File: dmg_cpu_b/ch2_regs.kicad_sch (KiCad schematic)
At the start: 96 parts

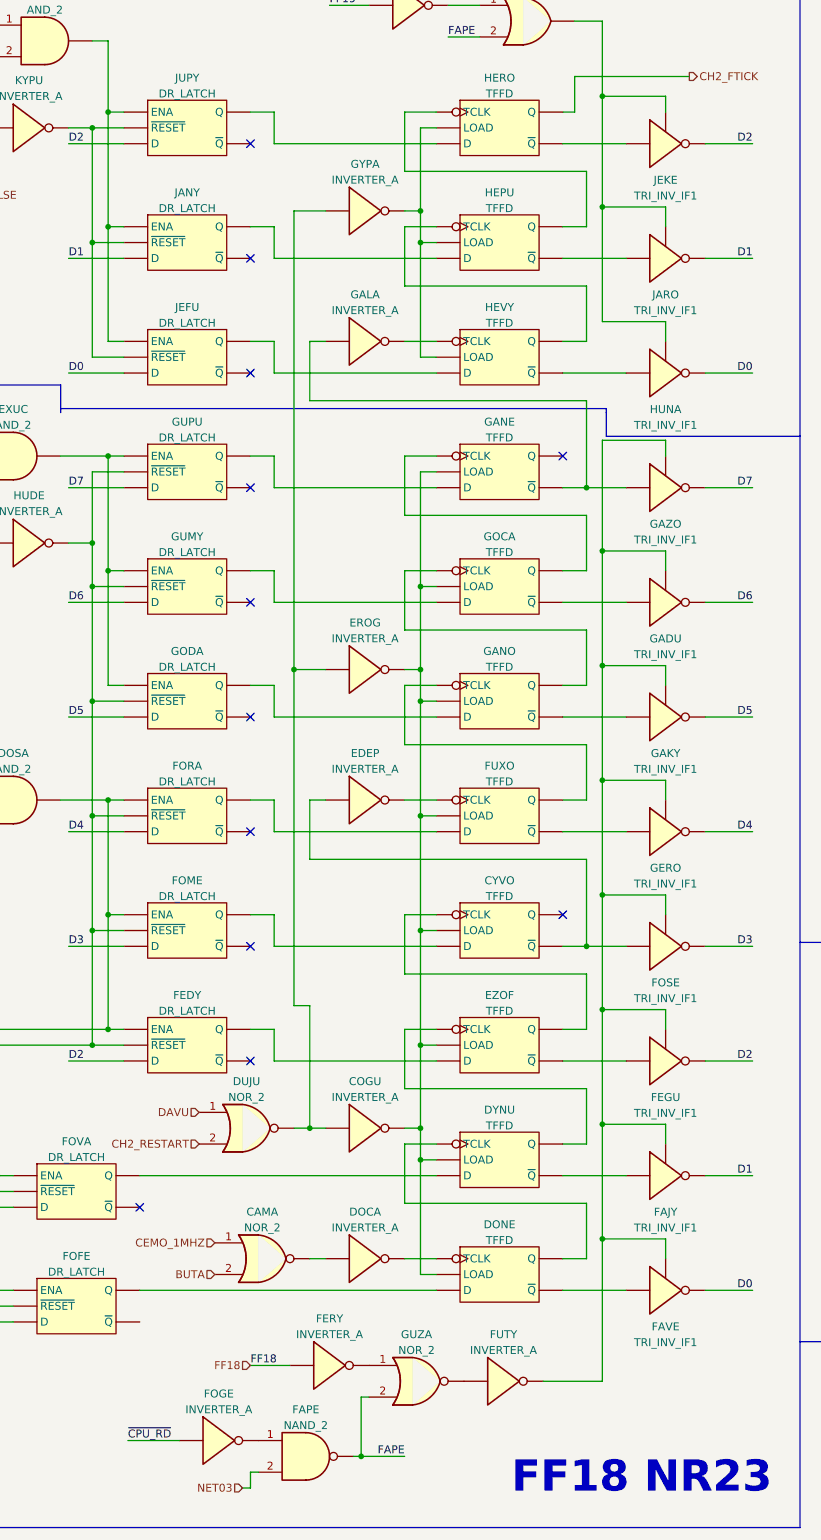
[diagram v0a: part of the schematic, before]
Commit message: Channel 2 + Channel 3 added. Channel 3 fits on 2 sheets.
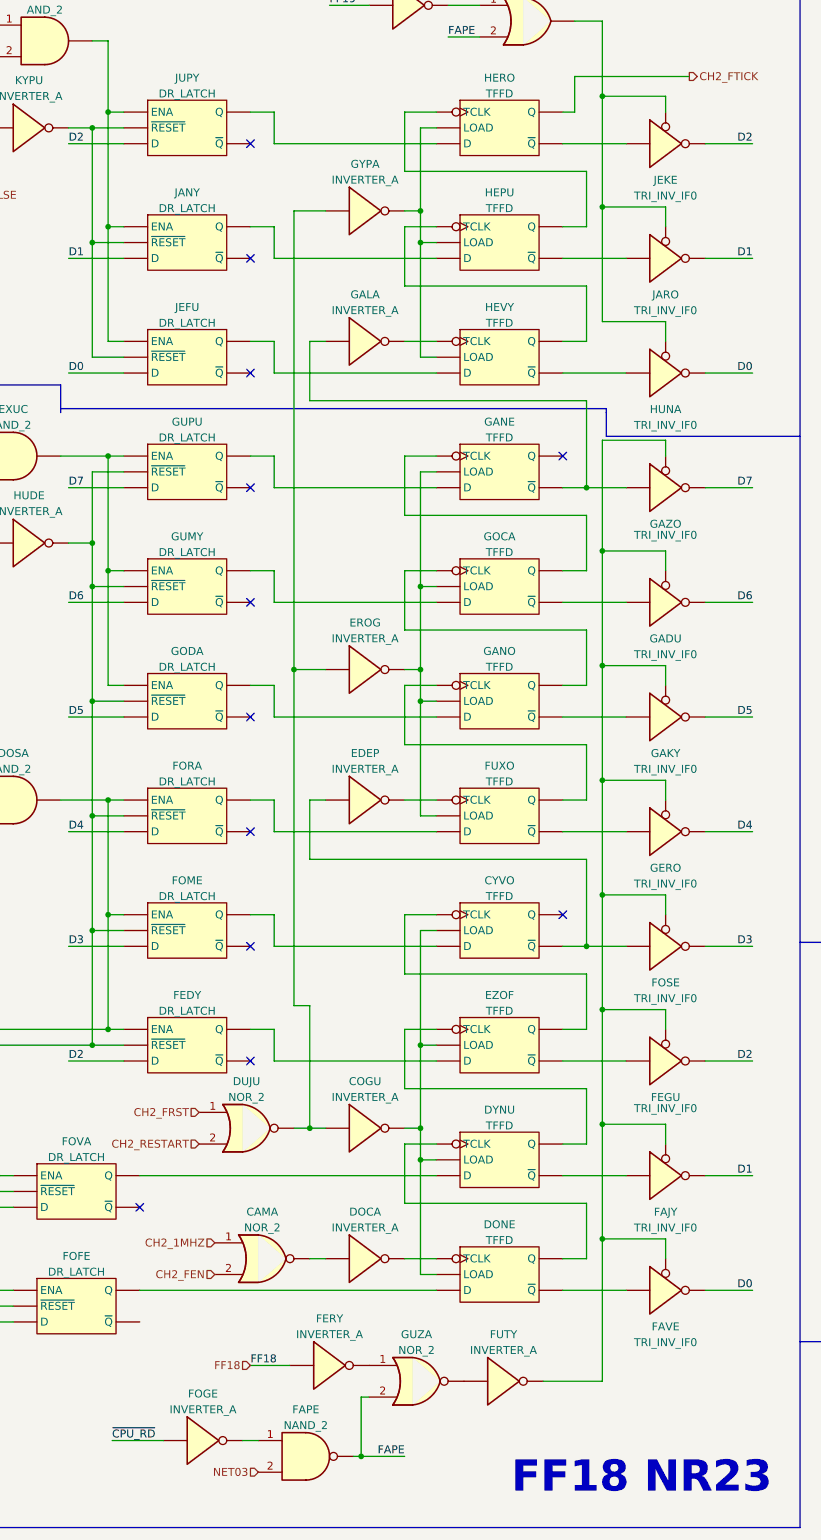
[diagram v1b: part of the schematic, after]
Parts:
- removed FAJY, FAVE, FEGU, FOSE, GADU, GAKY, GAZO, GERO, HUNA, JARO, JEKE: TRI_INV_IF1, symbol DMG_CPU_Cells:TRI_INV_IF1
- added FAJY, FAVE, FEGU, FOSE, GADU, GAKY, GAZO, GERO, HUNA, JARO, JEKE: TRI_INV_IF0, symbol DMG_CPU_Cells:TRI_INV_IF0
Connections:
- net D0: now also FAVE.3, HUNA.3
- net D1: now also FAJY.3, JARO.3
- net D2: now also FEGU.3, JEKE.3
- net D3: now also FOSE.3
- net D4: now also GERO.3
- net D5: now also GAKY.3
- net D6: now also GADU.3
- net D7: now also GAZO.3
- net at EROG.2, FUXO.3 (LOAD), FUXO.4 (LOAD)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: no longer COGU.2, CYVO.3 (LOAD), CYVO.4 (LOAD), DONE.3 (LOAD), DONE.4 (LOAD), DYNU.3 (LOAD), DYNU.4 (LOAD), EZOF.3 (LOAD), EZOF.4 (LOAD)
- net at GOCA.6 (~{Q}): now also GADU.2
- net at FUTY.2: now also FAJY.1 (~{ENA}), FAVE.1 (~{ENA}), FEGU.1 (~{ENA}), FOSE.1 (~{ENA}), GADU.1 (~{ENA}), GAKY.1 (~{ENA}), GAZO.1 (~{ENA}), GERO.1 (~{ENA})
- net at GANO.6 (~{Q}): now also GAKY.2
- net at GALA.1, GANE.6 (~{Q}): now also GAZO.2
- net at HYPO.3: now also HUNA.1 (~{ENA}), JARO.1 (~{ENA}), JEKE.1 (~{ENA})
- net at HERO.6 (~{Q}): now also JEKE.2
- net at CYVO.6 (~{Q}), EDEP.1: now also FOSE.2
- net at EZOF.6 (~{Q}): now also FEGU.2
- net at DONE.6 (~{Q}): now also FAVE.2
- net at HEPU.6 (~{Q}): now also JARO.2
- net at DYNU.6 (~{Q}): now also FAJY.2
- net at HEVY.6 (~{Q}): now also HUNA.2
- net at FUXO.6 (~{Q}): now also GERO.2
- net BUTA renamed CH2_FEN
- net CEMO_1MHZ renamed CH2_1MHZ
- net DAVU renamed CH2_FRST
- new net: COGU.2, CYVO.3 (LOAD), CYVO.4 (LOAD), DONE.3 (LOAD), DONE.4 (LOAD), DYNU.3 (LOAD), DYNU.4 (LOAD), EZOF.3 (LOAD), EZOF.4 (LOAD)
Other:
- moved on the sheet: FOGE

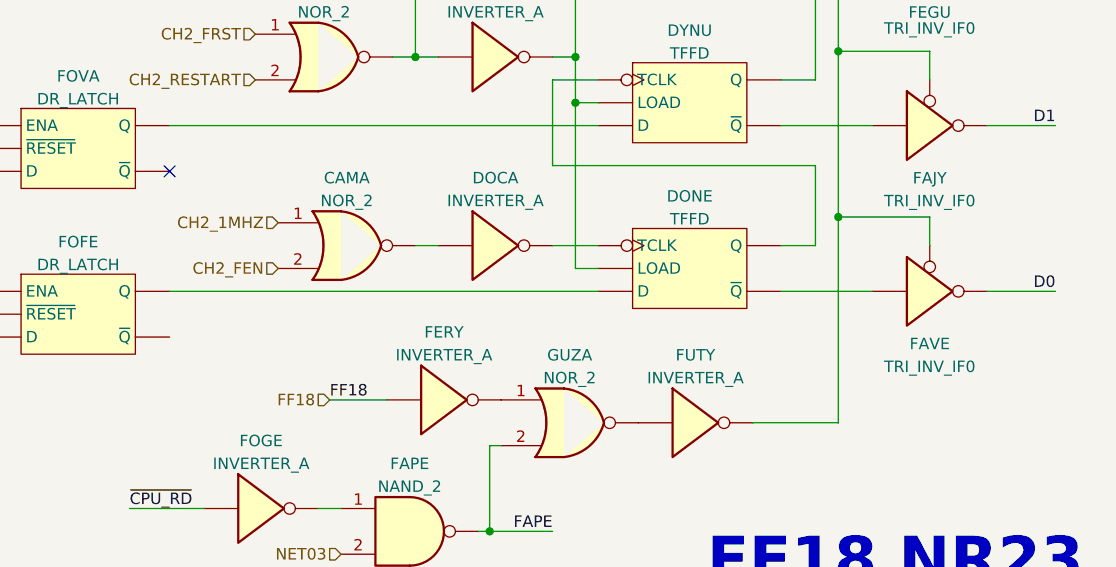
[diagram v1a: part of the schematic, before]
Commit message: Fixes made from issues, channel 4 sheet aded and tidy up of hierarchical APU sheet. Small fixes done here and there when doing ERC.
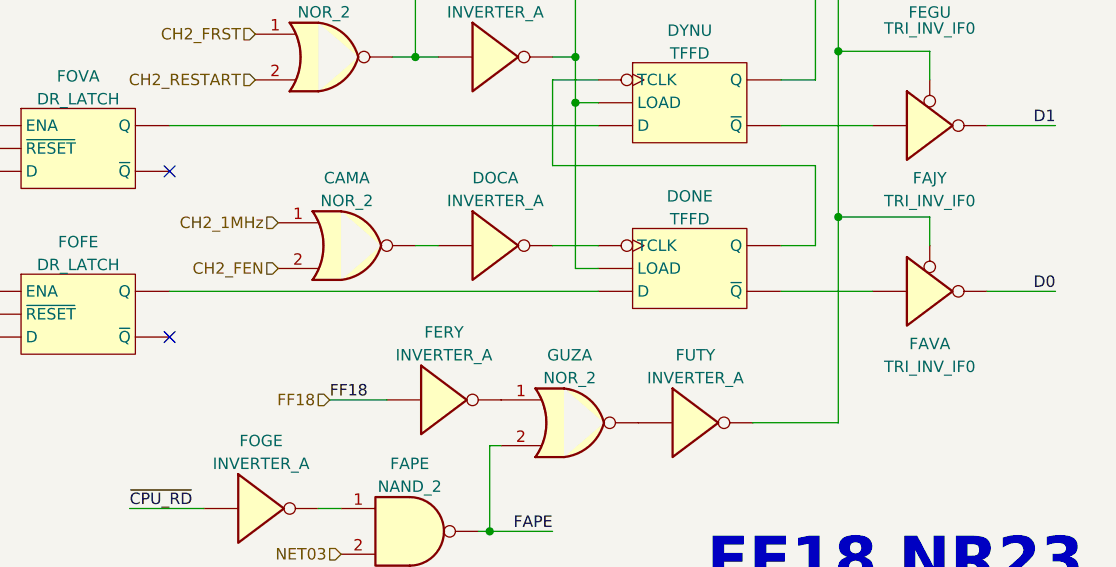
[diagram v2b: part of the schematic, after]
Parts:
- renumbered FAVE to FAVA
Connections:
- net CH2_1MHZ renamed CH2_1MHz
- no-connect marks 14 -> 15
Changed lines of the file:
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@@
   (no_connect (at 205.74 203.2))
   (no_connect (at 205.74 55.88))
+  (no_connect (at 187.96 245.11))
   (no_connect (at 205.74 166.37))
   (no_connect (at 255.905 106.045))
@@
     (effects (font (size 1.27 1.27)) (justify left))
   )
-  (hierarchical_label "CH2_1MHZ" (shape input) (at 200.025 232.41 180)
+  (hierarchical_label "CH2_1MHz" (shape input) (at 200.025 232.41 180)
     (effects (font (size 1.27 1.27)) (justify right))
   )
@@
   (symbol (lib_id "DMG_CPU_Cells:TRI_INV_IF0") (at 272.415 240.03 0) (unit 1)
     (in_bom yes) (on_board yes) (fields_autoplaced)
-    (property "Reference" "FAVE" (id 0) (at 272.415 245.8704 0))
+    (property "Reference" "FAVA" (id 0) (at 272.415 245.8704 0))
     (property "Value" "TRI_INV_IF0" (id 1) (at 272.415 248.4073 0))
     (property "Footprint" "" (id 2) (at 269.875 240.03 0)

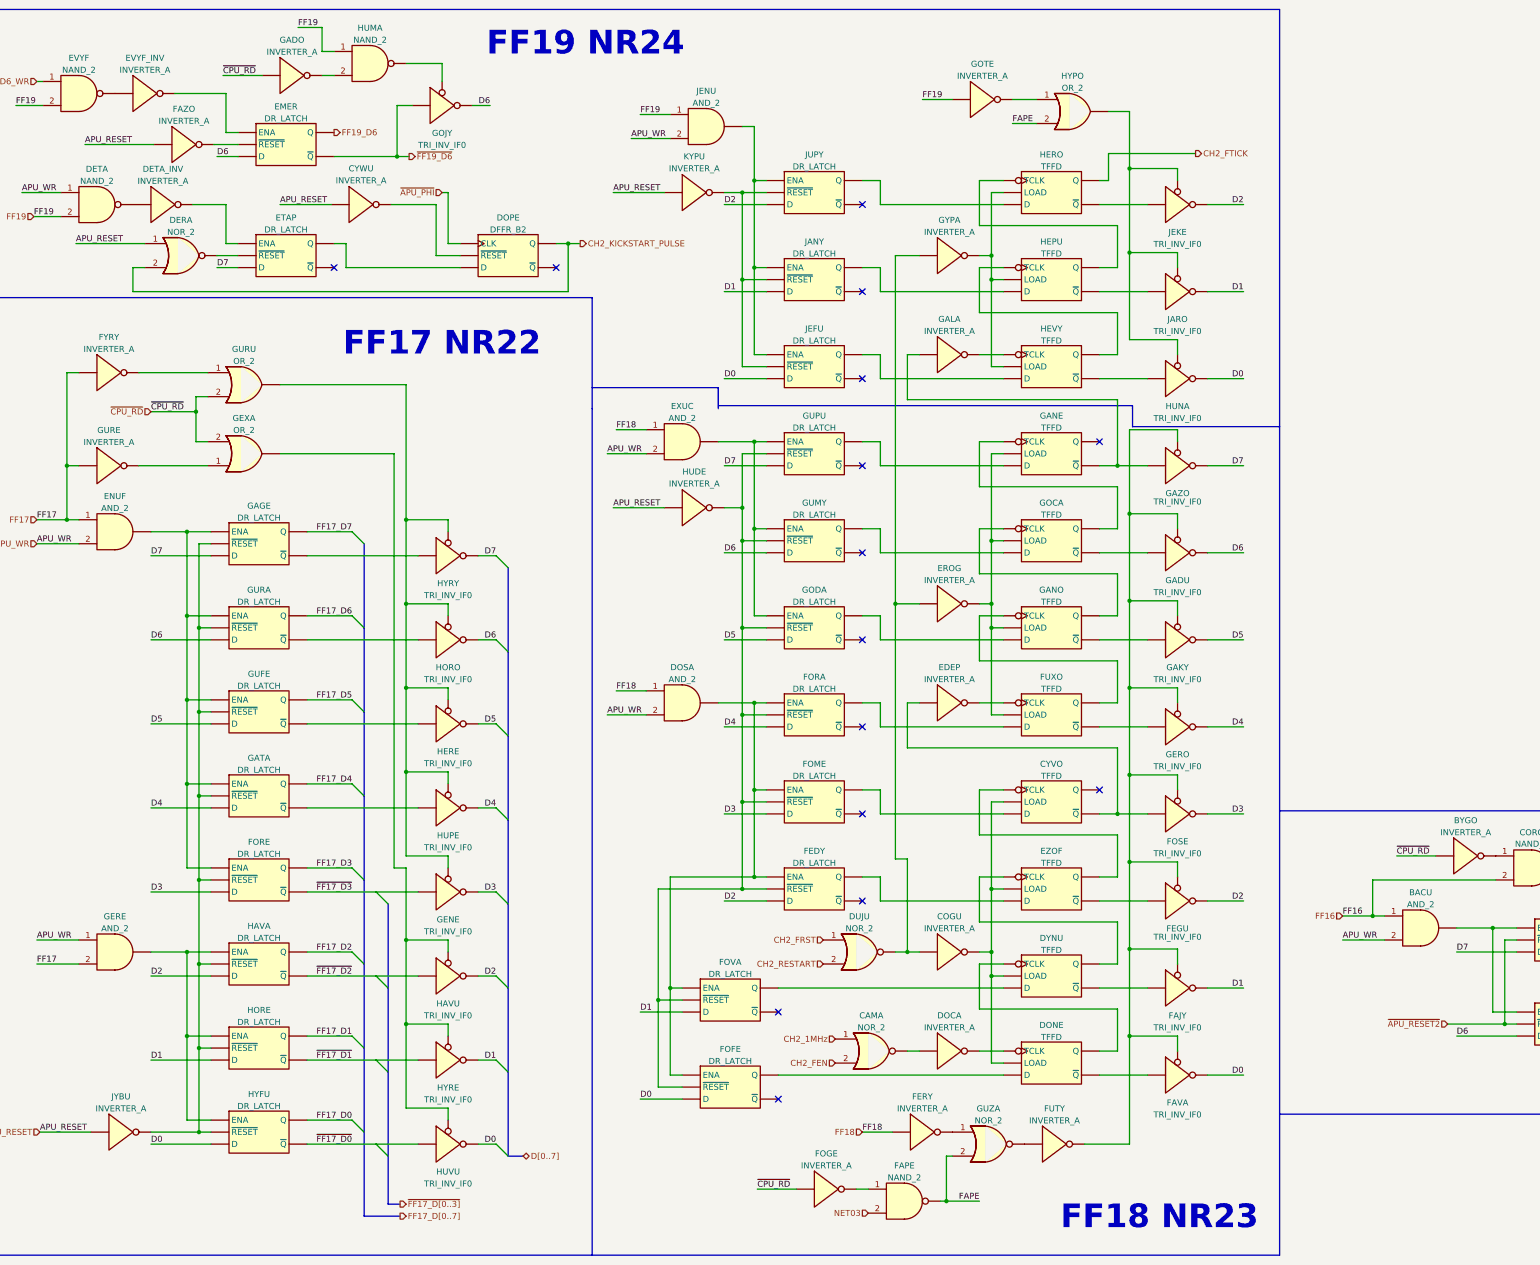
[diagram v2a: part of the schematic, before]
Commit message: Fixes made based on raised issues. PPU decode page added as draft level.
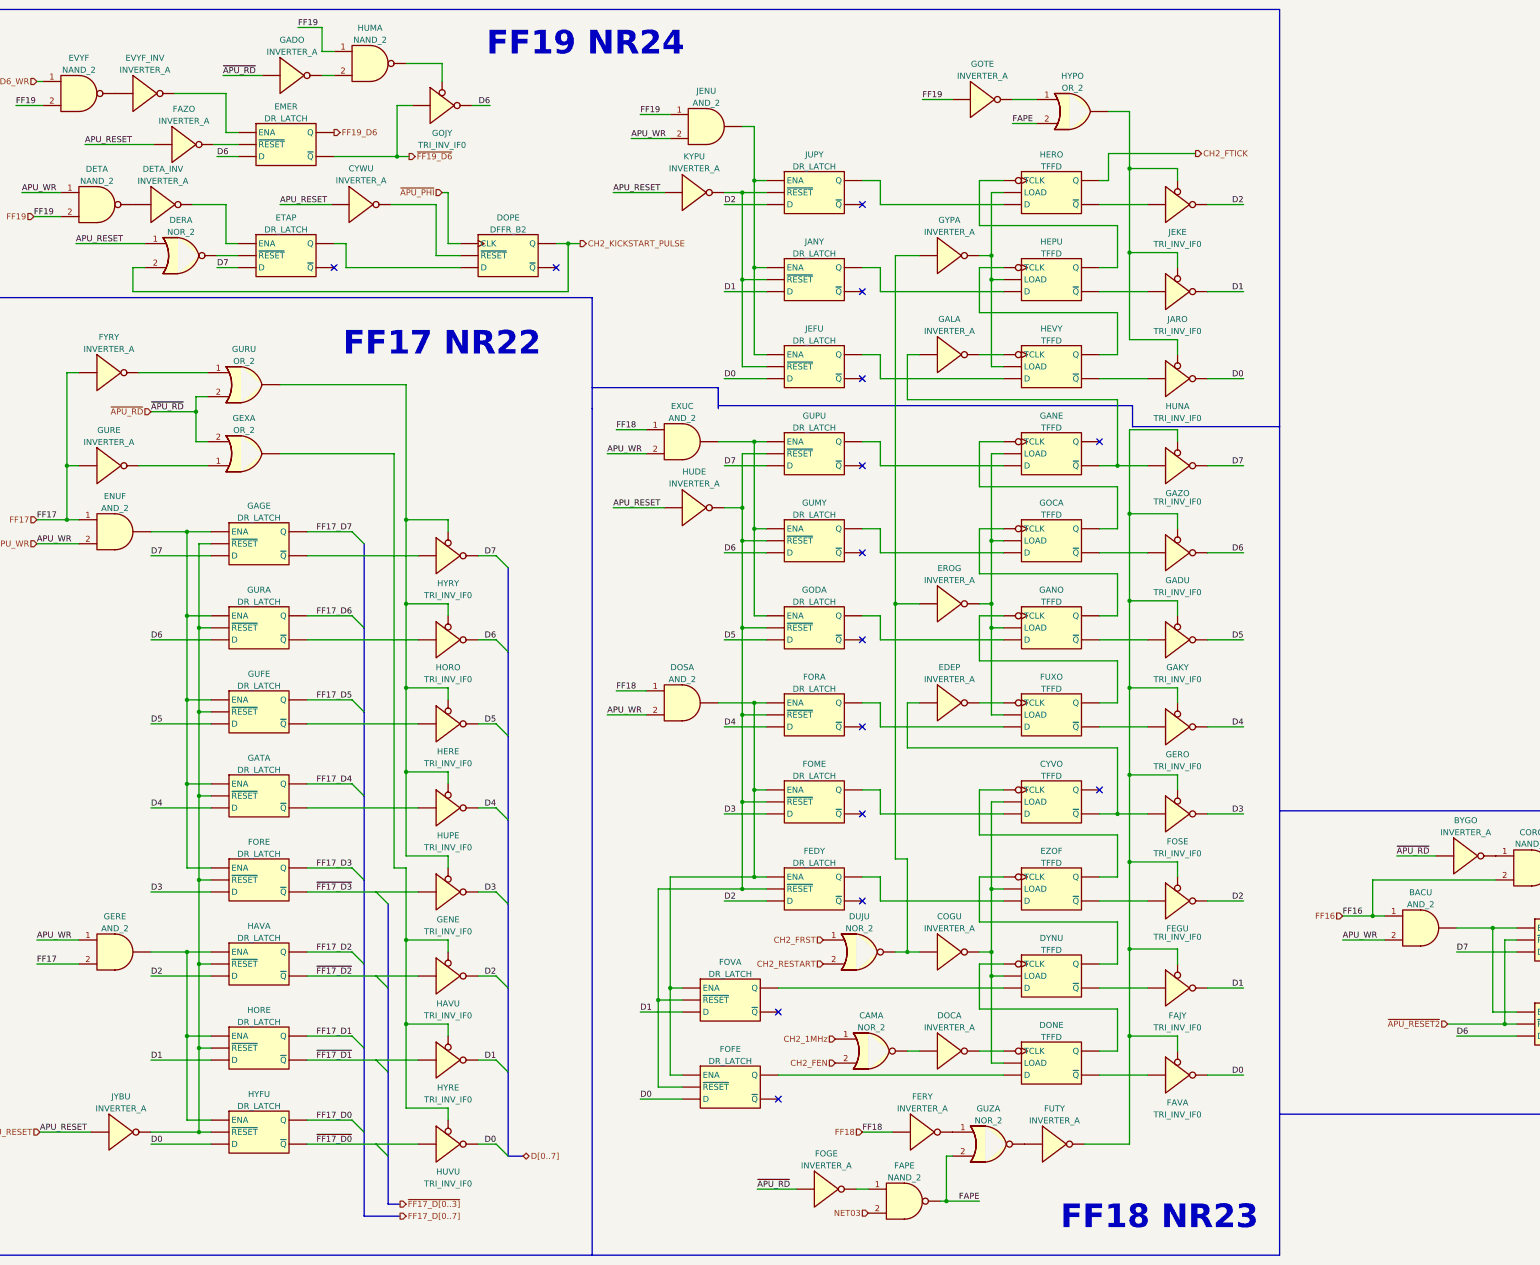
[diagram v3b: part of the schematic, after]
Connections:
- net ~{CPU_RD} renamed ~{APU_RD}
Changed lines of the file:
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@@
     (effects (font (size 1.27 1.27)) (justify left bottom))
   )
-  (label "~{CPU_RD}" (at 70.485 28.575 0)
+  (label "~{APU_RD}" (at 70.485 28.575 0)
     (effects (font (size 1.27 1.27)) (justify left bottom))
   )
@@
     (effects (font (size 1.27 1.27)) (justify left bottom))
   )
-  (label "~{CPU_RD}" (at 55.245 99.695 0)
-    (effects (font (size 1.27 1.27)) (justify left bottom))
-  )
-  (label "~{CPU_RD}" (at 183.515 264.16 0)
-    (effects (font (size 1.27 1.27)) (justify left bottom))
-  )
-  (label "~{CPU_RD}" (at 318.77 193.675 0)
+  (label "~{APU_RD}" (at 55.245 99.695 0)
+    (effects (font (size 1.27 1.27)) (justify left bottom))
+  )
+  (label "~{APU_RD}" (at 183.515 264.16 0)
+    (effects (font (size 1.27 1.27)) (justify left bottom))
+  )
+  (label "~{APU_RD}" (at 318.77 193.675 0)
     (effects (font (size 1.27 1.27)) (justify left bottom))
   )
@@
     (effects (font (size 1.27 1.27)) (justify right))
   )
-  (hierarchical_label "~{CPU_RD}" (shape input) (at 55.245 99.695 180)
-    (effects (font (size 1.27 1.27)) (justify right))
-  )
+  (hierarchical_label "~{APU_RD}" (shape input) (at 55.245 99.695 180)
+    (effects (font (size 1.27 1.27)) (justify right))
+  )

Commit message: Further fixes made based on raised issues.
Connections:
- net CH2_FEN renamed CH2_FDIS
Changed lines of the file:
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@@
     (effects (font (size 1.27 1.27)) (justify left))
   )
-  (hierarchical_label "CH2_FEN" (shape input) (at 200.025 237.49 180)
+  (hierarchical_label "CH2_FDIS" (shape input) (at 200.025 237.49 180)
     (effects (font (size 1.27 1.27)) (justify right))
   )

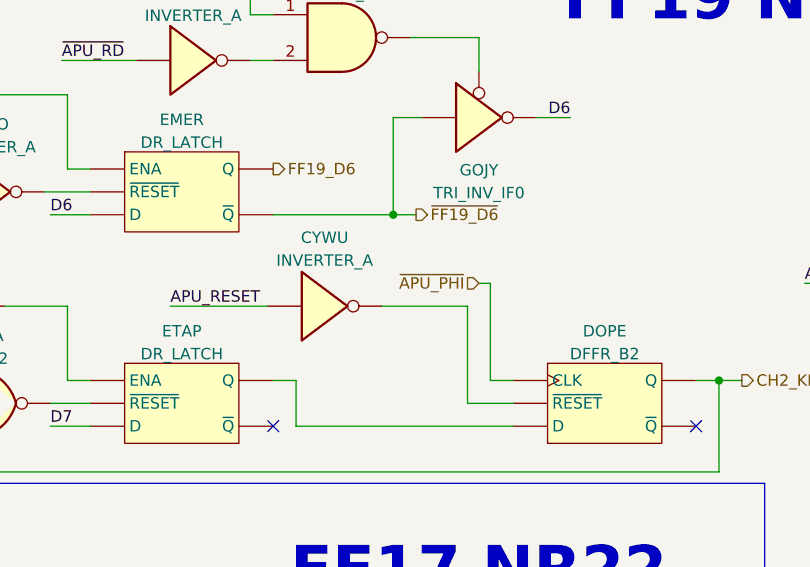
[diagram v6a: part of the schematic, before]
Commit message: Fixed PHI signals.
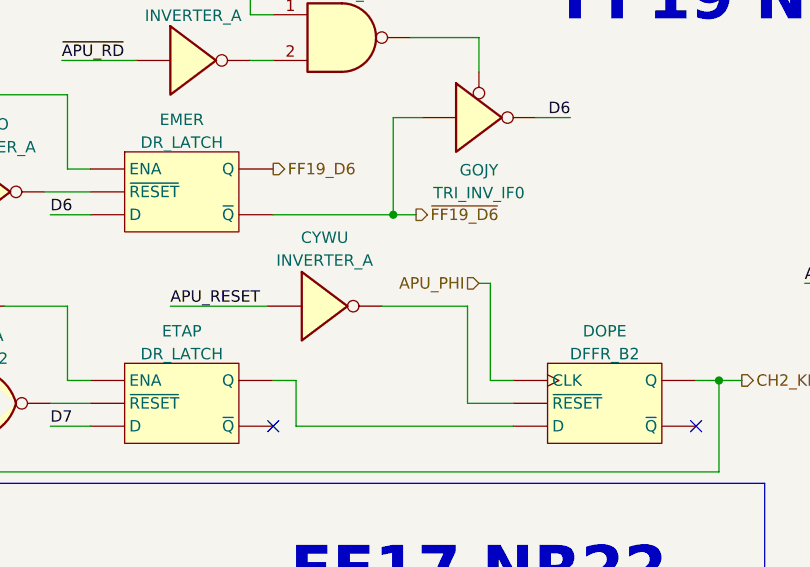
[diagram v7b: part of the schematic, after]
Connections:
- net ~{APU_PHI} renamed APU_PHI
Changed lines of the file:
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@@
     (effects (font (size 1.27 1.27)) (justify left))
   )
-  (hierarchical_label "~{APU_PHI}" (shape input) (at 116.84 53.34 180)
+  (hierarchical_label "APU_PHI" (shape input) (at 116.84 53.34 180)
     (effects (font (size 1.27 1.27)) (justify right))
   )
